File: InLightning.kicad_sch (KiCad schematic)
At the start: 2 parts, among them U1 NRF52832-QFAB-R, U2 MCP3564R-E/ST

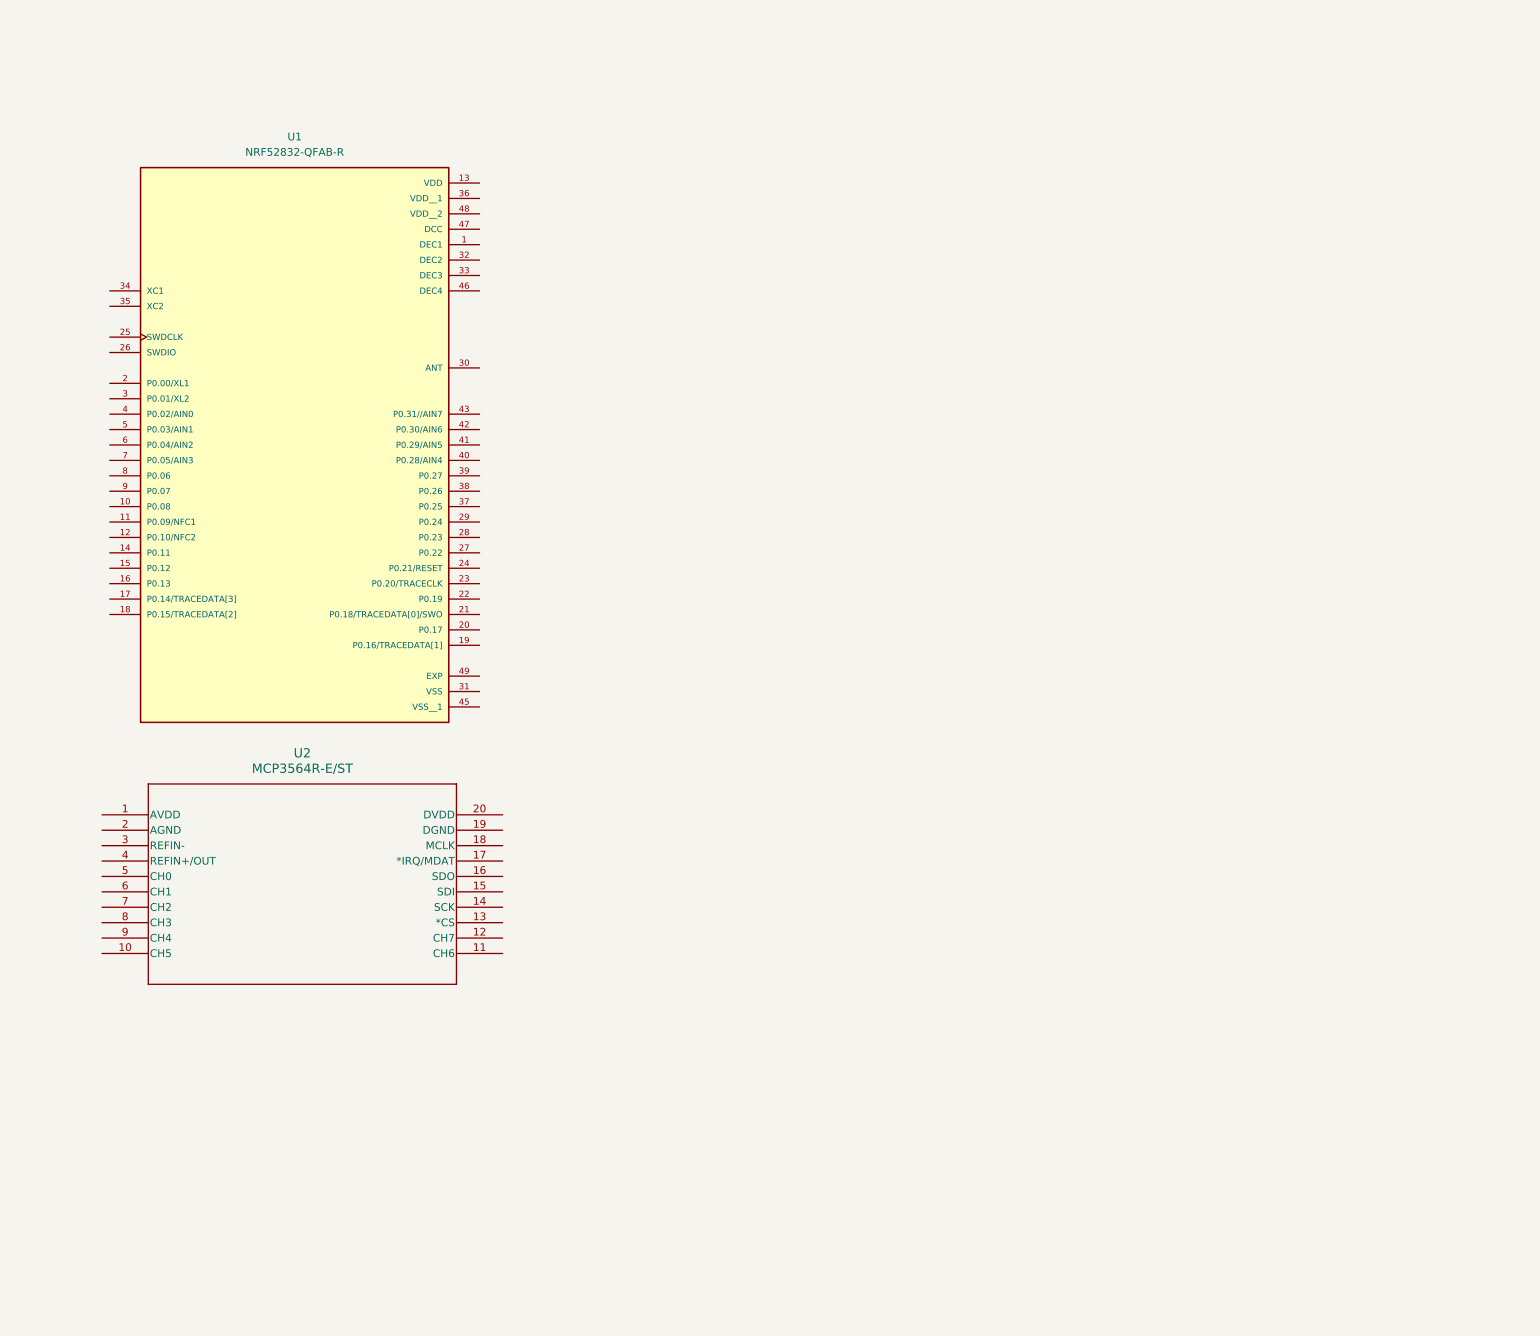
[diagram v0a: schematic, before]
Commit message: mcu schematics started
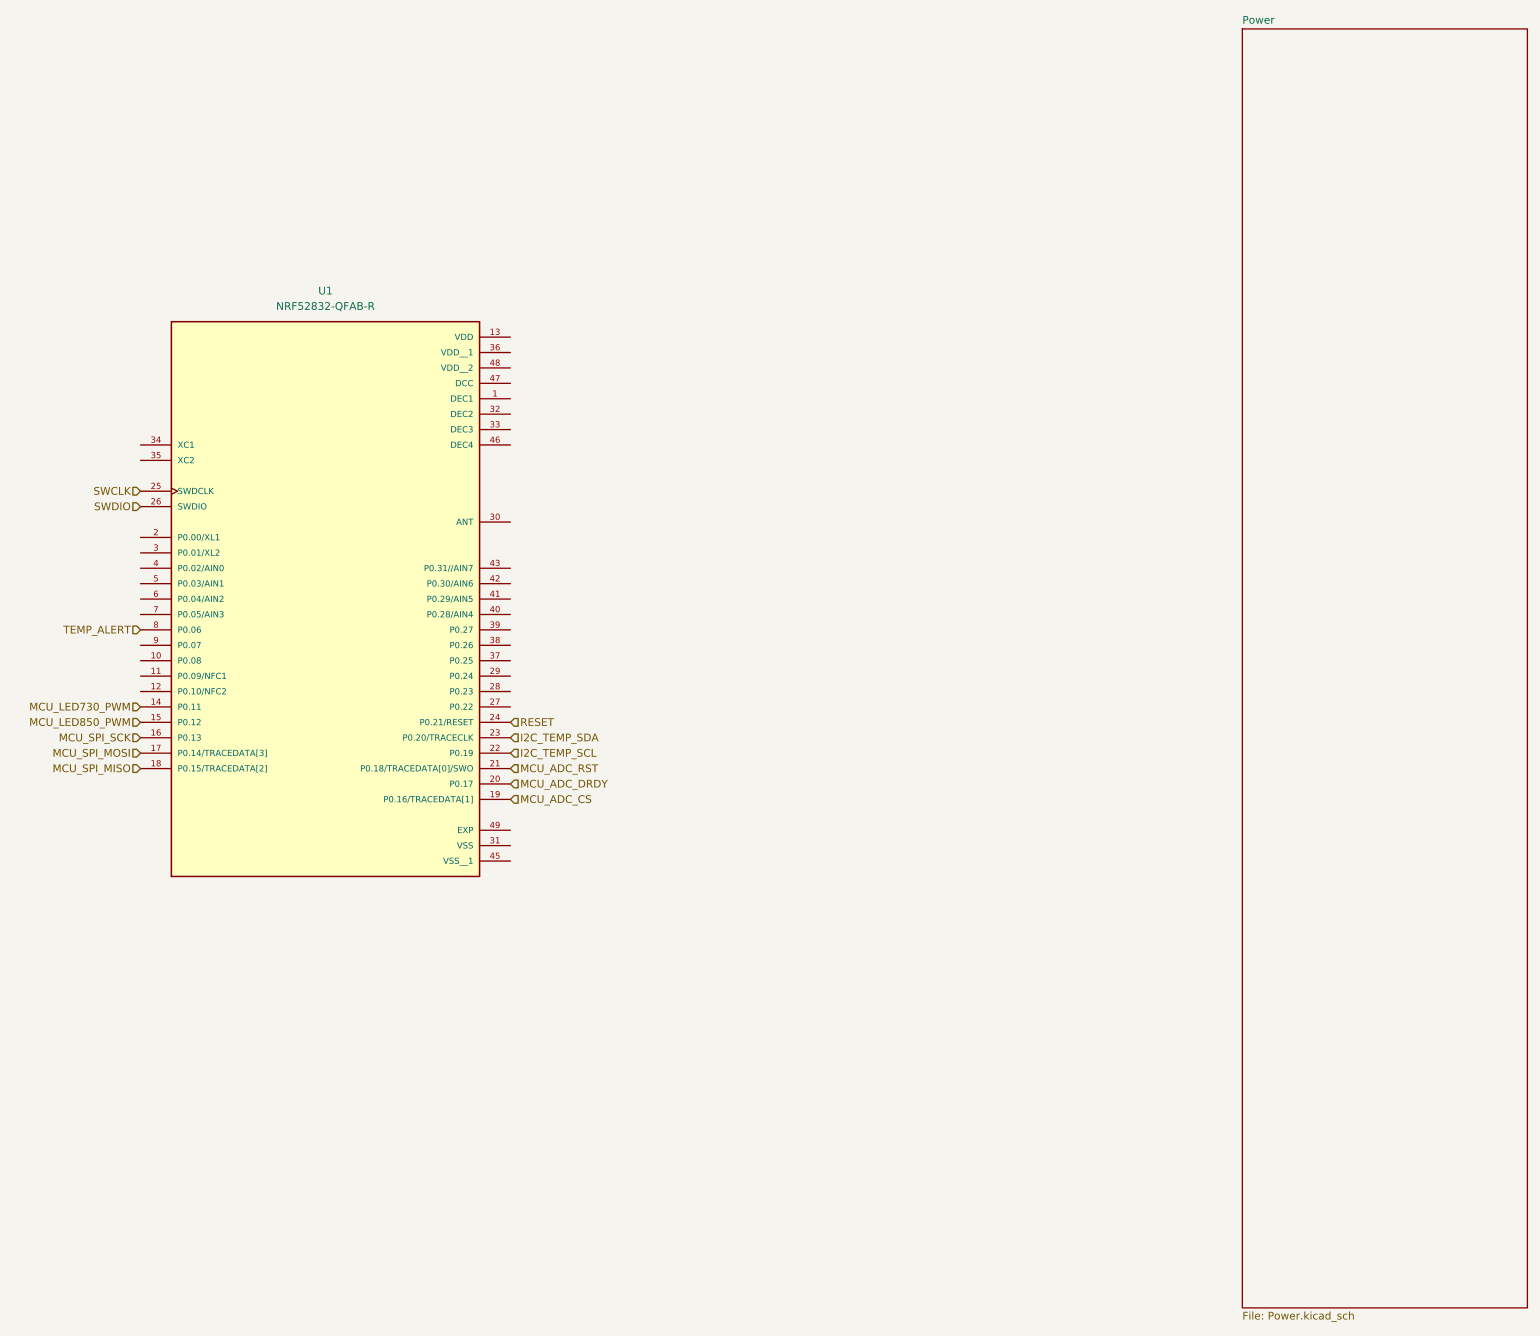
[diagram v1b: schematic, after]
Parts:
- removed U2: MCP3564R-E/ST, TSSOP20_ST_MCH, symbol MCP3564R_E_ST:MCP3564R-E_ST
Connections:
- net MCU_LED730_PWM: now reaches U1.14 (P0.11)
- net MCU_LED850_PWM: now reaches U1.15 (P0.12)
- net MCU_SPI_SCK: now reaches U1.16 (P0.13)
- net MCU_SPI_MOSI: now reaches U1.17 (P0.14/TRACEDATA[3])
- net MCU_SPI_MISO: now reaches U1.18 (P0.15/TRACEDATA[2])
- net MCU_ADC_CS: now reaches U1.19 (P0.16/TRACEDATA[1])
- net MCU_ADC_DRDY: now reaches U1.20 (P0.17)
- net MCU_ADC_RST: now reaches U1.21 (P0.18/TRACEDATA[0]/SWO)
- net I2C_TEMP_SCL: now reaches U1.22 (P0.19)
- net I2C_TEMP_SDA: now reaches U1.23 (P0.20/TRACECLK)
- net RESET: now reaches U1.24 (P0.21/RESET)
- net SWCLK: now reaches U1.25 (SWDCLK)
- net SWDIO: now reaches U1.26 (SWDIO)
- net TEMP_ALERT: now reaches U1.8 (P0.06)
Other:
- added sheet Power (Power.kicad_sch)
- title: (none) -> MCU
- moved on the sheet: U1
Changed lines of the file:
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@@
 	(generator_version "10.0")
 	(paper "A4")
-	(symbol
-		(lib_id "MCP3564R_E_ST:MCP3564R-E_ST")
-		(at 111.76 128.27 0)
-		(unit 1)
-		(body_style 1)
-		(exclude_from_sim no)
-		(in_bom yes)
-		(on_board yes)
-		(in_pos_files yes)
-		(dnp no)
-		(fields_autoplaced yes)
-		(property "Reference" "U2"
-			(at 144.78 118.11 0)
-			(show_name no)
-			(do_not_autoplace no)
-			(effects
-				(font
-					(size 1.524 1.524)
-				)
-			)
-		)
-		(property "Value" "MCP3564R-E/ST"
-			(at 144.78 120.65 0)
-			(show_name no)
-			(do_not_autoplace no)
-			(effects
-				(font
-					(size 1.524 1.524)
-				)
-			)
-		)
-		(property "Footprint" "TSSOP20_ST_MCH"
-			(at 111.76 128.27 0)
-			(hide yes)
-			(show_name no)
-			(do_not_autoplace no)
-			(effects
-				(font
-					(size 1.27 1.27)
-					(italic yes)
-				)
-			)
-		)
-		(property "Datasheet" "MCP3564R-E/ST"
-			(at 111.76 128.27 0)
-			(hide yes)
-			(show_name no)
-			(do_not_autoplace no)
-			(effects
-				(font
-					(size 1.27 1.27)
-					(italic yes)
-				)
-			)
-		)
-		(property "Description" ""
-			(at 111.76 128.27 0)
-			(hide yes)
-			(show_name no)
-			(do_not_autoplace no)
-			(effects
-				(font
-					(size 1.27 1.27)
-				)
-			)
-		)
-		(pin "12"
-		)
-		(pin "19"
-		)
-		(pin "3"
-		)
-		(pin "7"
-		)
-		(pin "4"
-		)
-		(pin "5"
-		)
-		(pin "13"
-		)
-		(pin "17"
-		)
-		(pin "18"
-		)
-		(pin "10"
-		)
-		(pin "11"
-		)
-		(pin "16"
-		)
-		(pin "14"
-		)
-		(pin "6"
-		)
-		(pin "1"
-		)
-		(pin "9"
-		)
-		(pin "2"
-		)
-		(pin "8"
-		)
-		(pin "15"
-		)
-		(pin "20"
-		)
-		(instances
-			(project "InLightning"
-				(path "/1aacc45f-6fcc-4559-bec0-55c6f50555c1"
-					(reference "U2")
-					(unit 1)
-				)
-			)
+	(title_block
+		(title "MCU")
+		(rev "0.1")
+	)
+	(hierarchical_label "MCU_LED730_PWM"
+		(shape input)
+		(at 118.11 110.49 180)
+		(effects
+			(font
+				(size 1.27 1.27)
+			)
+			(justify right)
+		)
+	)
+	(hierarchical_label "MCU_SPI_MISO"
+		(shape input)
+		(at 118.11 120.65 180)
+		(effects
+			(font
+				(size 1.27 1.27)
+			)
+			(justify right)
+		)
+	)
+	(hierarchical_label "MCU_ADC_CS"
+		(shape input)
+		(at 179.07 125.73 0)
+		(effects
+			(font
+				(size 1.27 1.27)
+			)
+			(justify left)
+		)
+	)
+	(hierarchical_label "MCU_ADC_RST"
+		(shape input)
+		(at 179.07 120.65 0)
+		(effects
+			(font
+				(size 1.27 1.27)
+			)
+			(justify left)
+		)
+	)
+	(hierarchical_label "MCU_SPI_SCK"
+		(shape input)
+		(at 118.11 115.57 180)
+		(effects
+			(font
+				(size 1.27 1.27)
+			)
+			(justify right)
+		)
+	)
+	(hierarchical_label "TEMP_ALERT"
+		(shape input)
+		(at 118.11 97.79 180)
+		(effects
+			(font
+				(size 1.27 1.27)
+			)
+			(justify right)
+		)
+	)
+	(hierarchical_label "MCU_LED850_PWM"
+		(shape input)
+		(at 118.11 113.03 180)
+		(effects
+			(font
+				(size 1.27 1.27)
+			)
+			(justify right)
+		)
+	)
+	(hierarchical_label "SWCLK"
+		(shape input)
+		(at 118.11 74.93 180)
+		(effects
+			(font
+				(size 1.27 1.27)
+			)
+			(justify right)
+		)
+	)
+	(hierarchical_label "RESET"
+		(shape input)
+		(at 179.07 113.03 0)
+		(effects
+			(font
+				(size 1.27 1.27)
+			)
+			(justify left)
+		)
+	)
+	(hierarchical_label "I2C_TEMP_SDA"
+		(shape input)
+		(at 179.07 115.57 0)
+		(effects
+			(font
+				(size 1.27 1.27)
+			)
+			(justify left)
+		)
+	)
+	(hierarchical_label "SWDIO"
+		(shape input)
+		(at 118.11 77.47 180)
+		(effects
+			(font
+				(size 1.27 1.27)
+			)
+			(justify right)
+		)
+	)
+	(hierarchical_label "I2C_TEMP_SCL"
+		(shape input)
+		(at 179.07 118.11 0)
+		(effects
+			(font
+				(size 1.27 1.27)
+			)
+			(justify left)
+		)
+	)
+	(hierarchical_label "MCU_SPI_MOSI"
+		(shape input)
+		(at 118.11 118.11 180)
+		(effects
+			(font
+				(size 1.27 1.27)
+			)
+			(justify right)
+		)
+	)
+	(hierarchical_label "MCU_ADC_DRDY"
+		(shape input)
+		(at 179.07 123.19 0)
+		(effects
+			(font
+				(size 1.27 1.27)
+			)
+			(justify left)
 		)
 	)
 	(symbol
 		(lib_id "NRF52832-QFAB-R:NRF52832-QFAB-R")
-		(at 143.51 62.23 0)
+		(at 148.59 87.63 0)
 		(unit 1)
 		(body_style 1)
@@
 		(fields_autoplaced yes)
 		(property "Reference" "U1"
-			(at 143.51 16.51 0)
+			(at 148.59 41.91 0)
 			(show_name no)
 			(do_not_autoplace no)
@@
 		)
 		(property "Value" "NRF52832-QFAB-R"
-			(at 143.51 19.05 0)
+			(at 148.59 44.45 0)
 			(show_name no)
 			(do_not_autoplace no)
@@
 		)
 		(property "Footprint" "NRF52832-QFAB-R:QFN40P600X600X90-49N"
-			(at 143.51 62.23 0)
+			(at 148.59 87.63 0)
 			(hide yes)
 			(show_name no)
@@
 		)
 		(property "Datasheet" ""
-			(at 143.51 62.23 0)
+			(at 148.59 87.63 0)
 			(hide yes)
 			(show_name no)
@@
 		)
 		(property "Description" ""
-			(at 143.51 62.23 0)
+			(at 148.59 87.63 0)
 			(hide yes)
 			(show_name no)
@@
 		)
 		(property "PARTREV" "1.4"
-			(at 143.51 62.23 0)
+			(at 148.59 87.63 0)
 			(hide yes)
 			(show_name no)
@@
 		)
 		(property "MANUFACTURER" "Nordic Semiconductor"
-			(at 143.51 62.23 0)
+			(at 148.59 87.63 0)
 			(hide yes)
 			(show_name no)
@@
 		)
 		(property "MAXIMUM_PACKAGE_HEIGHT" "0.9mm"
-			(at 143.51 62.23 0)
+			(at 148.59 87.63 0)
 			(hide yes)
 			(show_name no)
@@
 		)
 		(property "STANDARD" "IPC 7351B"
-			(at 143.51 62.23 0)
+			(at 148.59 87.63 0)
 			(hide yes)
 			(show_name no)
@@
 				)
 			)
+		)
+	)
+	(sheet
+		(at 299.72 -1.27)
+		(size 46.99 210.82)
+		(exclude_from_sim no)
+		(in_bom yes)
+		(on_board yes)
+		(dnp no)
+		(fields_autoplaced yes)
+		(stroke
+			(width 0.1524)
+			(type solid)
+		)
+		(fill
+			(color 0 0 0 0)
+		)
+		(property "Sheetname" "Power"
+			(at 299.72 -1.9816 0)
+			(show_name no)
+			(do_not_autoplace no)
+			(effects
+				(font
+					(size 1.27 1.27)
+				)
+				(justify left bottom)
+			)
+		)
+		(property "Sheetfile" "Power.kicad_sch"
+			(at 299.72 210.1346 0)
+			(show_name no)
+			(do_not_autoplace no)
+			(effects
+				(font
+					(size 1.27 1.27)
+				)
+				(justify left top)
+			)
+		)
+		(instances
+			(project "InLightning"
+				(path "/1aacc45f-6fcc-4559-bec0-55c6f50555c1"
+					(page "2")
+				)
+			)
